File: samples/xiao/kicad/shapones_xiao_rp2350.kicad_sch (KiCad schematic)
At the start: 44 parts, among them Q1 PMOS, Q4 NMOS, SW1 POWER, SW10 MENU, SW2 A, SW3 B, SW4 SELECT, SW5 START, SW6 UP, SW7 DOWN, SW8 LEFT, SW9 RIGHT, U1 XIAO RP2350, U2 PCA9555D, U4 1.54''IPS-240x240, U5 TFCard, U6 74AHC1G04W5, U7 HT82V73A

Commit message: wip: PCB layout
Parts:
- removed BT1: Battery_Cell, symbol Device:Battery_Cell
- removed C6: 1u, symbol Device:C_Small
- removed LS1: 8ohm, symbol Device:Speaker
- removed SW1: POWER, symbol Switch:SW_Push
- removed SW10: MENU, symbol Switch:SW_Push
- removed SW2: A, symbol Switch:SW_Push
- removed SW3: B, symbol Switch:SW_Push
- removed SW4: SELECT, symbol Switch:SW_Push
- removed SW5: START, symbol Switch:SW_Push
- removed SW6: UP, symbol Switch:SW_Push
- removed SW7: DOWN, symbol Switch:SW_Push
- removed SW8: LEFT, symbol Switch:SW_Push
- removed SW9: RIGHT, symbol Switch:SW_Push
- removed U1: XIAO RP2350, symbol shpc_modules:RaspberryPiPico
- removed U2: PCA9555D, Package_SO:SOIC-24W_7.5x15.4mm_P1.27mm, symbol Interface_Expansion:PCA9555D
- removed U4: 1.54''IPS-240x240, symbol shpc_modules:RaspberryPiPico
- removed U5: TFCard, symbol shpc_modules:RaspberryPiPico
- removed U6: 74AHC1G04W5, Package_TO_SOT_SMD:SOT-553, symbol 74xGxx:74LVC1GU04DRL
- removed U7: HT82V73A, Package_SO:JEITA_SOIC-8_3.9x4.9mm_P1.27mm, symbol Amplifier_Audio:IS31AP4991-GRLS2
- added C11, C4: 1u, Capacitor_SMD:C_0402_1005Metric, symbol Device:C_Small
- added C2: 4.7u, Capacitor_SMD:C_0603_1608Metric, symbol Device:C_Small
- added C5: 4.7u, Capacitor_SMD:C_0402_1005Metric, symbol Device:C_Small
- added D4, D6, D8: 1N4148WS, Diode_SMD:D_SOD-323, symbol Device:D_Small
- added D5: YLED0402B, LED_SMD:LED_0402_1005Metric, symbol Device:LED_Small
- added D9: YLED0402O, LED_SMD:LED_0402_1005Metric, symbol Device:LED_Small
- added FB2: BLM21PG331SN1D, Inductor_SMD:L_Walsin_WLFM201209x, symbol Device:FerriteBead_Small
- added J1: JST S2B-PH-SM4-TB, Connector_JST:JST_PH_S2B-PH-SM4-TB_1x02-1MP_P2.00mm_Horizontal, symbol Connector_Generic_MountingPin:Conn_01x02_MountingPin
- added J3: Micro_SD_Card_Det_Hirose_DM3AT, Connector_Card:microSD_HC_Hirose_DM3AT-SF-PEJM5, symbol Connector:Micro_SD_Card_Det_Hirose_DM3AT
- added J4: Hong Cheng HC-PM254-5.0H-2x10PS, Connector_PinSocket_2.54mm:PinSocket_2x10_P2.54mm_Vertical_SMD, symbol Connector_Generic:Conn_02x10_Odd_Even
- added J5, J6: Conn_01x01, Connector_Wire:SolderWirePad_1x01_SMD_2x4mm, symbol Connector_Generic:Conn_01x01
- added Q2: IRLML6344TRPBF, Package_TO_SOT_SMD:SOT-23, symbol Simulation_SPICE:NMOS
- added Q4: IRLML2246TRPBF, Package_TO_SOT_SMD:SOT-23, symbol Simulation_SPICE:PMOS
- added R11, R23, R24, R25: 0, Resistor_SMD:R_0402_1005Metric, symbol Device:R_Small
- added R16, R21, R42, R5, R8: 10k, Resistor_SMD:R_0402_1005Metric, symbol Device:R_Small
- added R18: 2.2k, Resistor_SMD:R_0402_1005Metric, symbol Device:R_Small
- added R2, R9: 100, Resistor_SMD:R_0402_1005Metric, symbol Device:R_Small
- added R20: 22k, Resistor_SMD:R_0402_1005Metric, symbol Device:R_Small
- added R22, R7: 100k, Resistor_SMD:R_0402_1005Metric, symbol Device:R_Small
- added RV1: RK10J12E0A0A, shpc_mechanical:RK10J1xE, symbol shpc_mechanical:RK10J12E0A0A
- added SW1, SW10: GT-TC018A-H0375-L1, shpc_mechanical:GT-TC018A-H0375-L1, symbol Switch:SW_Push_Shielded
- added SW2, SW3, SW4, SW5, SW6, SW7, SW8, SW9: Rubber, shpc_mechanical:Rubber_Contact, symbol shpc_mechanical:Rubber_Contact
- added U1: XIAO RP2350, shpc_modules:XIAO RP2350, symbol shpc_modules:XIAO_RP2350
- added U2: RT9080-33GJ5, Package_TO_SOT_SMD:TSOT-23-5, symbol shpc_ic:RT9080-33GJ5
- added U3: 74VHC1G126, Package_TO_SOT_SMD:SOT-23-5, symbol shpc_ic:MC74VHC1G126DTT1G-TP
- added U4: HT82V73A, shpc_ic:SOIC-8_with_Thermal_Hole, symbol shpc_ic:HT82V73A
- added U5: PCA9555PW, Package_SO:TSSOP-24_4.4x7.8mm_P0.65mm, symbol Interface_Expansion:PCA9555PW
- added U6: M154-240240-RGB, shpc_modules:M154-240240-RGB, symbol shpc_modules:M154-240240-RGB
- C1: footprint (none) -> Capacitor_SMD:C_0603_1608Metric
- C10: renamed from C3; footprint (none) -> Capacitor_SMD:C_0402_1005Metric
- C3: renamed from C2; footprint (none) -> Capacitor_SMD:C_0402_1005Metric
- C6: renamed from C4; footprint (none) -> Capacitor_SMD:C_0402_1005Metric
- C7: renamed from C5; footprint (none) -> Capacitor_SMD:C_0402_1005Metric
- C8: renamed from C7; footprint (none) -> Capacitor_SMD:C_0603_1608Metric
- C9: renamed from C8; footprint (none) -> Capacitor_SMD:C_0603_1608Metric
- D1, D2, D3: value 1N4148W -> 1N4148WS; footprint (none) -> Diode_SMD:D_SOD-323; LCSC (none) -> C60580
- Q1: renamed from Q4; value NMOS -> IRLML6344TRPBF; footprint (none) -> Package_TO_SOT_SMD:SOT-23; LCSC (none) -> C53550
- Q3: renamed from Q1; value PMOS -> IRLML2246TRPBF; footprint (none) -> Package_TO_SOT_SMD:SOT-23; LCSC (none) -> C127272
- R1, R4: footprint (none) -> Resistor_SMD:R_0402_1005Metric
- R12: renamed from R8; footprint (none) -> Resistor_SMD:R_0402_1005Metric
- R13: renamed from R9; footprint (none) -> Resistor_SMD:R_0402_1005Metric; now not fitted
- R14: renamed from R10; footprint (none) -> Resistor_SMD:R_0402_1005Metric; now not fitted
- R15: renamed from R11; footprint (none) -> Resistor_SMD:R_0402_1005Metric; now not fitted
- R17: renamed from R12; footprint (none) -> Resistor_SMD:R_0402_1005Metric
- R19: renamed from R25; footprint (none) -> Resistor_SMD:R_0402_1005Metric
- R26, R28: value 10k -> 0; footprint (none) -> Resistor_SMD:R_0402_1005Metric
- R27: value 2.2k -> 0; footprint (none) -> Resistor_SMD:R_0402_1005Metric; now not fitted
- R3: renamed from R2; footprint (none) -> Resistor_SMD:R_0402_1005Metric
- R6: renamed from R3; footprint (none) -> Resistor_SMD:R_0402_1005Metric
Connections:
- net MISO is gone; now on net LCD_CS: R12.2
- net +3V3: now also R27.1, C2.1, J4.2 (Pin_2), R23.1, R25.1, SW1.1, U1.12 (3V3), U5.24 (VDD)
- net GND: now also D3.2 (A), R26.2, C11.2, C4.2, C5.2, D5.1 (K), J1.MP (MountPin), J3.11 (SHIELD), J3.6 (VSS), J4.17 (Pin_17), J4.4 (Pin_4), Q2.3 (S), R22.2, R24.2, R7.2, RV1.1, RV1.2B, RV1.3B, SW1.SH (B), SW10.2, SW10.SH (B), SW2.2, SW3.2, SW4.2, SW5.2, SW6.2, SW7.2, SW8.2, SW9.2, U1.13 (GND), U2.2 (GND), U2.4 (NC), U3.3 (GND), U4.4 (VSS), U5.12 (VSS), U6.1 (GND), U6.MP; no longer D2.2 (A), R27.2
- net LCD_CS: now also J4.11 (Pin_11), U1.4 (GP5), U6.7 (CS); no longer R17.2
- net LCD_DC: now also J4.10 (Pin_10), U1.3 (GP28), U6.6 (DC)
- net SOUND: now also U1.8 (GP1), U3.2
- net SW_DOWN: now also D2.1 (K), SW4.1, U5.18 (IO1_5); no longer D3.1 (K)
- net VPERI: now also J3.4 (VDD), J4.1 (Pin_1), R16.1, R21.1, R8.1, U2.3 (EN), U6.2 (VCC), U6.8 (BLK); no longer C6.2, C8.2
- net at D1.1 (K), R1.1, R3.1: now also R2.2, SW1.2
- net at R4.2: now also D2.2 (A); no longer D3.2 (A)
- net at R28.1: now also R27.2, U5.3 (A2)
- net at C9.2: now also U4.3 (VREF)
- net at C1.1, D1.2 (A), Q1.2 (G)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: now also D3.1 (K); no longer D2.1 (K)
- net at C7.1, R19.2: now also R18.2, R20.1; no longer R26.1
- net at R19.1: now also U3.4
- net BOOTSEL: no longer names the net of R4.1
- net BOOTSEL: now also U1.15 (BOOT)
- net CLK renamed SPI_MOSI
- net SPI_MOSI: now also J3.3 (CMD), J4.8 (Pin_8), U1.11 (GP3), U6.4 (SDA)
- net MOSI renamed SPI_SCK
- net SPI_SCK: now also J3.5 (CLK), J4.7 (Pin_7), U1.9 (GP2), U6.3 (SCL)
- net PERI_EN: no longer names the net of Q3.2 (G), R6.2
- net PERI_EN: now also C2.2, D4.2 (A), Q2.1 (D)
- net RESET: no longer names the net of Q1.1 (D)
- net RESET: now also U1.16 (RST)
- net TF_CS: no longer names the net of R13.2
- net TF_CS: now also R11.2, U6.5 (RES)
- new net: J6.1 (Pin_1), U4.1
- new net: RV1.2A, U4.2 (IN)
- new net: D8.1 (K), R22.1, R42.2, U4.5 (~{CE})
- new net: J5.1 (Pin_1), U4.7
- new net: Q2.2 (G), R5.1, R7.1
- new net: R20.2, RV1.3A
- new net: C11.1, FB2.2, U2.1 (VIN)
- new net: D9.2 (A), R21.2
- new net: R23.2, R24.1, U5.21 (A0)
- new net: Q4.2 (G), R9.2
- new net: R25.2, R26.1, U5.2 (A1)
- new net: D5.2 (A), R8.2
- new net: R2.1, U1.2 (GP27)
- new net +BAT: J1.1 (Pin_1), Q4.1 (D), U1.18 (BAT+)
- new net -BAT: J1.2 (Pin_2), U1.17 (BAT-)
- new net EXT_AUDIO: J4.20 (Pin_20), R18.1
- new net EXT_MUTE: D8.2 (A), J4.19 (Pin_19)
- new net I2C_SCL: J4.12 (Pin_12), R5.2, U1.6 (GP7), U5.22 (SCL)
- new net I2C_SDA: J4.13 (Pin_13), U1.5 (GP6), U5.23 (SDA)
- new net IOEX0: J4.14 (Pin_14), U5.4 (IO0_0)
- new net IOEX1: J4.15 (Pin_15), U5.5 (IO0_1)
- new net IOEX2: J4.16 (Pin_16), U5.6 (IO0_2)
- new net IOEX3: J4.18 (Pin_18), U5.7 (IO0_3)
- new net LCD_RESET_N: R11.1, U5.9 (IO0_5)
- new net MUTE_INT: R42.1, U5.10 (IO0_6)
- new net PERI_EN_N: D4.1 (K), U5.8 (IO0_4)
- new net SPI_MISO: J3.7 (DAT0), J4.9 (Pin_9), R17.2, U1.10 (GP4)
- new net SW_A: SW9.1, U5.13 (IO1_0)
- new net SW_B: SW8.1, U5.14 (IO1_1)
- new net SW_LEFT: SW3.1, U5.19 (IO1_6)
- new net SW_MENU: SW10.1, U5.11 (IO0_7)
- new net SW_RIGHT: SW2.1, U5.20 (IO1_7)
- new net SW_SELECT: SW7.1, U5.15 (IO1_2)
- new net SW_START: SW6.1, U5.16 (IO1_3)
- new net SW_UP: SW5.1, U5.17 (IO1_4)
- new net TFC_CS: D9.1 (K), J3.2 (DAT3/CD), R16.2, U1.7 (GP0)
- new net VANL: C5.1, C6.2, C8.2, U2.5 (VOUT), U3.1, U3.5 (VCC), U4.8 (VDD)
- new net VBUS: D6.2 (A), J4.6 (Pin_6), R9.1, U1.14 (VBUS)
- new net VCOM: C4.1, D6.1 (K), FB2.1, J4.3 (Pin_3), Q4.3 (S)
- new net XIAO_GPIO: J4.5 (Pin_5), U1.1 (GP26)
- no-connect marks 7 -> 5
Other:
- note added: "A"
- note added: "B"
- note added: "BATTERY"
- note added: "DOWN"
- note added: "EXT_PORT"
- note added: "LEFT"
- note added: "MENU"
- note added: "POWER"
- note added: "RIGHT"
- note added: "SELECT"
- note added: "SPEAKER"
- note added: "START"
- note added: "UP"
- moved on the sheet: C1, C10, C3, C6, C7, C8, C9, D1, Q1, Q3, R1, R12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

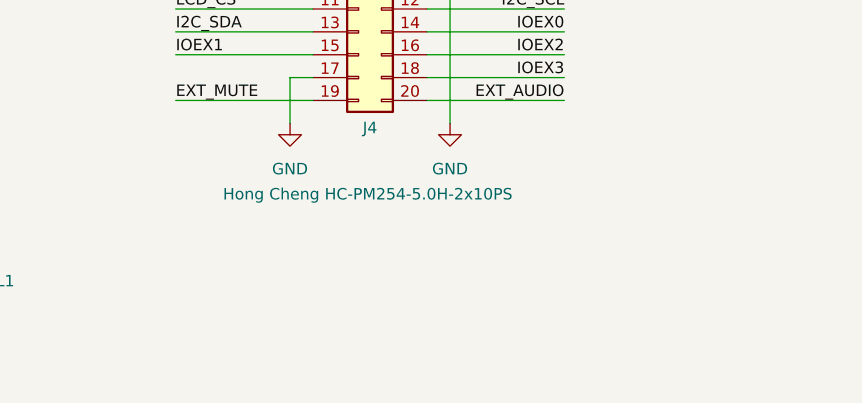
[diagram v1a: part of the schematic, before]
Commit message: add tooling strips
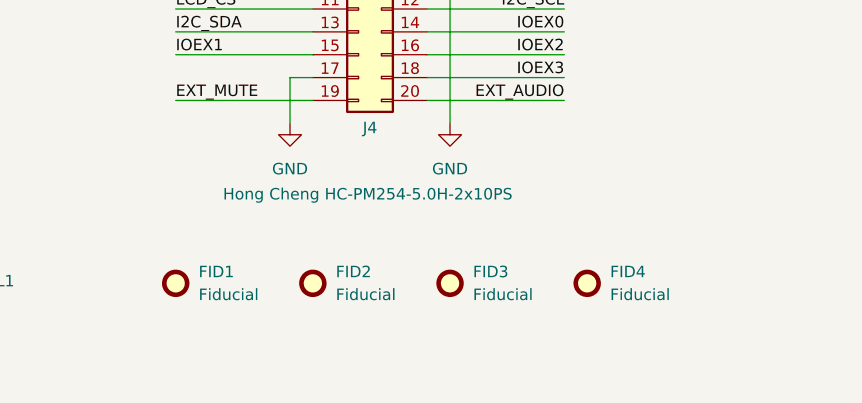
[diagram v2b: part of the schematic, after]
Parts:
- added FID1, FID2, FID3, FID4: Fiducial, Fiducial:Fiducial_1mm_Mask2mm, symbol Mechanical:Fiducial
- C1, C2: LCSC (none) -> C1705; URL (none) -> https://www.lcsc.com/product-detail/C1705.html
- C10, C6: LCSC (none) -> C1525; URL (none) -> https://www.lcsc.com/product-detail/C1525.html
- C11, C3, C4: LCSC (none) -> C14445; URL (none) -> https://www.lcsc.com/product-detail/C14445.html
- C5: footprint Capacitor_SMD:C_0402_1005Metric -> Capacitor_SMD:C_0603_1608Metric; LCSC (none) -> C1705; URL (none) -> https://www.lcsc.com/product-detail/C1705.html
- C7: LCSC (none) -> C15195; URL (none) -> https://www.lcsc.com/product-detail/C15195.html
- C8: LCSC (none) -> C140782; URL (none) -> https://www.lcsc.com/product-detail/C140782.html
- C9: LCSC (none) -> C1691; URL (none) -> https://www.lcsc.com/product-detail/C1691.html
- R1, R12, R13, R14, R16, R17, R21, R42, R5, R8: LCSC (none) -> C60490; URL (none) -> https://www.lcsc.com/product-detail/C60490.html
- R11, R23, R24, R25, R26, R27, R28: LCSC (none) -> C106231; URL (none) -> https://www.lcsc.com/product-detail/C106231.html
- R15: LCSC (none) -> C60489; URL (none) -> https://www.lcsc.com/product-detail/C60489.html
- R18, R19: LCSC (none) -> C114762; URL (none) -> https://www.lcsc.com/product-detail/C114762.html
- R2, R9: LCSC (none) -> C1545; URL (none) -> https://www.lcsc.com/product-detail/C1545.html
- R20: LCSC (none) -> C82868; URL (none) -> https://www.lcsc.com/product-detail/C82868.html
- R22, R6, R7: LCSC (none) -> C60491; URL (none) -> https://www.lcsc.com/product-detail/C60491.html
- R3: LCSC (none) -> C137976; URL (none) -> https://www.lcsc.com/product-detail/C137976.html
- R4: LCSC (none) -> C106235; URL (none) -> https://www.lcsc.com/product-detail/C106235.html

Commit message: Orders made to JLCPCB
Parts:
- removed FID1, FID2, FID3, FID4: Fiducial, Fiducial:Fiducial_1mm_Mask2mm, symbol Mechanical:Fiducial
- removed J5, J6: Conn_01x01, Connector_Wire:SolderWirePad_1x01_SMD_2x4mm, symbol Connector_Generic:Conn_01x01
- added J2: Conn_01x02, shpc_mechanical:SolderWirePad_1x02_SMD_150x50mil, symbol Connector_Generic:Conn_01x02
- D1, D2, D3, D4, D6, D8: URL (none) -> https://www.lcsc.com/product-detail/C60580.html
- D5: URL (none) -> https://www.lcsc.com/product-detail/C30584803.html
- D9: URL (none) -> https://www.lcsc.com/product-detail/C28310436.html
- FB2: footprint Inductor_SMD:L_Walsin_WLFM201209x -> Inductor_SMD:L_0805_2012Metric; URL (none) -> https://www.lcsc.com/product-detail/C74764.html
- J1: URL (none) -> https://www.lcsc.com/product-detail/C295747.html
- J3: URL (none) -> https://www.lcsc.com/product-detail/C114218.html
- J4: URL (none) -> https://www.lcsc.com/product-detail/C42163138.html
- Q1, Q2: URL (none) -> https://www.lcsc.com/product-detail/C53550.html
- Q3, Q4: URL (none) -> https://www.lcsc.com/product-detail/C127272.html
- R15: LCSC C60489 -> C60490; URL https://www.lcsc.com/product-detail/C60489.html -> https://www.lcsc.com/product-detail/C60490.html
- RV1: URL (none) -> https://www.lcsc.com/product-detail/C351176.html
- SW1, SW10: URL (none) -> https://www.lcsc.com/product-detail/C963235.html
- U2: URL (none) -> https://www.lcsc.com/product-detail/C841192.html
- U3: URL (none) -> https://www.lcsc.com/product-detail/C53100485.html
- U5: URL (none) -> https://www.lcsc.com/product-detail/C128392.html
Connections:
- net I2C_SCL: now also J4.13 (Pin_13); no longer J4.12 (Pin_12)
- net I2C_SDA: now also J4.12 (Pin_12); no longer J4.13 (Pin_13)
- net at U4.1: now also J2.2 (Pin_2)
- net at U4.7: now also J2.1 (Pin_1)
- net IOEX_A2: now reaches R27.2, R28.1, U5.3 (A2)
- net IOEX_A0: now reaches R23.2, R24.1, U5.21 (A0)
- net IOEX_A1: now reaches R25.2, R26.1, U5.2 (A1)
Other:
- moved on the sheet: R23, R24, R25, R26, R27, R28

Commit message: fix
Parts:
- R22: now fitted
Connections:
- net MUTE_INT renamed INT_MUTE
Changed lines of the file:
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@@
 		)
 	)
-	(label "MUTE_INT"
+	(label "INT_MUTE"
 		(at 88.9 154.94 0)
 		(effects
@@
 		)
 	)
-	(label "MUTE_INT"
+	(label "INT_MUTE"
 		(at 99.06 213.36 180)
 		(effects
@@
 		(in_bom yes)
 		(on_board yes)
-		(dnp yes)
+		(dnp no)
 		(property "Reference" "R22"
 			(at 120.65 137.16 90)

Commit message: fix
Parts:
- removed D4, D8: 1N4148WS, Diode_SMD:D_SOD-323, symbol Device:D_Small
- removed R42: 10k, Resistor_SMD:R_0402_1005Metric, symbol Device:R_Small
- added Q5: IRLML2246TRPBF, Package_TO_SOT_SMD:SOT-23, symbol Simulation_SPICE:PMOS
- added R10: 100k, Resistor_SMD:R_0402_1005Metric, symbol Device:R_Small
- added R29, R30: 10k, Resistor_SMD:R_0402_1005Metric, symbol Device:R_Small
- R5: value 10k -> 100k
- R7: value 100k -> 1M
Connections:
- net +3V3: now also R29.1, R30.1
- net EXT_MUTE: now also Q5.2 (G), R10.2
- net GND: now also R10.1; no longer Q2.3 (S), R22.2, R7.2
- net I2C_SCL: now also R29.2
- net I2C_SDA: now also R30.2
- net INT_MUTE: now also Q5.1 (D)
- net PERI_EN_N: now also Q2.3 (S), R7.2
- net VANL: now also R22.2
- net at R22.1, U4.5 (~{CE}): now also Q5.3 (S)
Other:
- moved on the sheet: C1, C11, C2, C3, C4, C5, D1, D2, D3, D5, D6, FB2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

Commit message: fix
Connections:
- net EXT_MUTE: no longer J4.19 (Pin_19), Q5.2 (G), R10.2
- net INT_MUTE renamed IOEX_MUTE
- new net SPK_MUTE: J4.19 (Pin_19), Q5.2 (G), R10.2
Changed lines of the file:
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@@
 		)
 	)
-	(label "INT_MUTE"
+	(label "IOEX_MUTE"
 		(at 99.06 213.36 180)
 		(effects
@@
 		)
 	)
-	(label "EXT_MUTE"
+	(label "SPK_MUTE"
 		(at 215.9 233.68 0)
 		(effects
@@
 		)
 	)
-	(label "EXT_MUTE"
+	(label "SPK_MUTE"
 		(at 88.9 154.94 0)
 		(effects
@@
 		)
 	)
-	(label "INT_MUTE"
+	(label "IOEX_MUTE"
 		(at 88.9 175.26 0)
 		(effects

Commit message: fix
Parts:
- removed R11: 0, Resistor_SMD:R_0402_1005Metric, symbol Device:R_Small
- added D4, D7: 1N4148WS, Diode_SMD:D_SOD-323, symbol Device:D_Small
- R13: now fitted
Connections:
- net IOEX_MUTE: now also D4.1 (K); no longer Q5.1 (D)
- net LCD_RESET_N: now also D7.1 (K)
- net at R13.2, U6.5 (RES): now also D7.2 (A)
- new net: D4.2 (A), Q5.1 (D)
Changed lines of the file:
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@@
 	(wire
 		(pts
-			(xy 88.9 175.26) (xy 115.57 175.26)
+			(xy 88.9 175.26) (xy 101.6 175.26)
 		)
 		(stroke
@@
 	(wire
 		(pts
+			(xy 106.68 175.26) (xy 115.57 175.26)
+		)
+		(stroke
+			(width 0)
+			(type default)
+		)
+	)
+	(wire
+		(pts
 			(xy 40.64 73.66) (xy 45.72 73.66)
 		)
@@
 	)
 	(symbol
-		(lib_id "power:+3V3")
-		(at 129.54 30.48 0)
+		(lib_id "Device:D_Small")
+		(at 195.58 121.92 0)
+		(mirror x)
 		(unit 1)
 		(exclude_from_sim no)
@@
 		(on_board yes)
 		(dnp no)
-		(fields_autoplaced yes)
-		(property "Reference" "#PWR06"
-			(at 129.54 34.29 0)
+		(property "Reference" "D7"
+			(at 194.056 124.714 0)
+			(effects
+				(font
+					(size 1.27 1.27)
+				)
+			)
+		)
+		(property "Value" "1N4148WS"
+			(at 197.866 126.746 0)
+			(effects
+				(font
+					(size 1.27 1.27)
+				)
+			)
+		)
+		(property "Footprint" "Diode_SMD:D_SOD-323"
+			(at 195.58 121.92 90)
 			(effects
 				(font
@@
 			)
 		)
-		(property "Value" "VBUS"
-			(at 129.54 25.4 0)
+		(property "Datasheet" "~"
+			(at 195.58 121.92 90)
 			(effects
 				(font
 					(size 1.27 1.27)
 				)
+				(hide yes)
 			)
 		)
-		(property "Footprint" ""
-			(at 129.54 30.48 0)
+		(property "Description" "Diode, small symbol"
+			(at 195.58 121.92 0)
 			(effects
 				(font
@@
 			)
 		)
-		(property "Datasheet" ""
-			(at 129.54 30.48 0)
+		(property "Sim.Device" "D"
+			(at 195.58 121.92 0)
 			(effects
 				(font
@@
 			)
 		)
-		(property "Description" "Power symbol creates a global label with name \"+3V3\""
-			(at 129.54 30.48 0)
+		(property "Sim.Pins" "1=K 2=A"
+			(at 195.58 121.92 0)
+			(effects
+				(font
+					(size 1.27 1.27)
+				)
+				(hide yes)
+			)
+		)
+		(property "LCSC" "C60580"
+			(at 195.58 121.92 0)
+			(effects
+				(font
+					(size 1.27 1.27)
+				)
+				(hide yes)
+			)
+		)
+		(property "URL" "https://www.lcsc.com/product-detail/C60580.html"
+			(at 195.58 121.92 0)
 			(effects
 				(font
@@
 			)
 		)
+		(pin "2"
+		)
 		(pin "1"
 		)
@@
 			(project "shapones_xiao_rp2350"
 				(path "/c325fb4c-906a-4010-8224-fd2c0e1f0539"
-					(reference "#PWR06")
+					(reference "D7")
 					(unit 1)
 				)
@@
 	)
 	(symbol
-		(lib_id "Device:R_Small")
-		(at 172.72 35.56 0)
-		(mirror y)
+		(lib_id "power:+3V3")
+		(at 129.54 30.48 0)
 		(unit 1)
 		(exclude_from_sim no)
@@
 		(on_board yes)
 		(dnp no)
-		(property "Reference" "R6"
-			(at 171.45 34.29 0)
-			(effects
-				(font
-					(size 1.016 1.016)
-				)
-				(justify left)
-			)
-		)
-		(property "Value" "100k"
-			(at 171.45 36.83 0)
-			(effects
-				(font
-					(size 1.27 1.27)
-				)
-				(justify left)
-			)
-		)
-		(property "Footprint" "Resistor_SMD:R_0402_1005Metric"
-			(at 172.72 35.56 0)
+		(fields_autoplaced yes)
+		(property "Reference" "#PWR06"
+			(at 129.54 34.29 0)
 			(effects
 				(font
@@
 			)
 		)
-		(property "Datasheet" "~"
-			(at 172.72 35.56 0)
+		(property "Value" "VBUS"
+			(at 129.54 25.4 0)
 			(effects
 				(font
 					(size 1.27 1.27)
 				)
-				(hide yes)
 			)
 		)
-		(property "Description" "Resistor, small symbol"
-			(at 172.72 35.56 0)
+		(property "Footprint" ""
+			(at 129.54 30.48 0)
 			(effects
 				(font
@@
 			)
 		)
-		(property "LCSC" "C60491"
-			(at 171.45 34.29 0)
+		(property "Datasheet" ""
+			(at 129.54 30.48 0)
 			(effects
 				(font
@@
 			)
 		)
-		(property "URL" "https://www.lcsc.com/product-detail/C60491.html"
-			(at 171.45 34.29 0)
+		(property "Description" "Power symbol creates a global label with name \"+3V3\""
+			(at 129.54 30.48 0)
 			(effects
 				(font
@@
 		(pin "1"
 		)
-		(pin "2"
-		)
 		(instances
 			(project "shapones_xiao_rp2350"
 				(path "/c325fb4c-906a-4010-8224-fd2c0e1f0539"
-					(reference "R6")
+					(reference "#PWR06")
 					(unit 1)
 				)
@@
 	(symbol
 		(lib_id "Device:R_Small")
-		(at 195.58 121.92 90)
+		(at 172.72 35.56 0)
+		(mirror y)
 		(unit 1)
 		(exclude_from_sim no)
@@
 		(on_board yes)
 		(dnp no)
-		(property "Reference" "R11"
-			(at 195.58 124.206 90)
+		(property "Reference" "R6"
+			(at 171.45 34.29 0)
 			(effects
 				(font
 					(size 1.016 1.016)
 				)
+				(justify left)
 			)
 		)
-		(property "Value" "0"
-			(at 195.58 126.492 90)
+		(property "Value" "100k"
+			(at 171.45 36.83 0)
 			(effects
 				(font
 					(size 1.27 1.27)
 				)
+				(justify left)
 			)
 		)
 		(property "Footprint" "Resistor_SMD:R_0402_1005Metric"
-			(at 195.58 121.92 0)
+			(at 172.72 35.56 0)
 			(effects
 				(font
@@
 		)
 		(property "Datasheet" "~"
-			(at 195.58 121.92 0)
+			(at 172.72 35.56 0)
 			(effects
 				(font
@@
 		)
 		(property "Description" "Resistor, small symbol"
-			(at 195.58 121.92 0)
+			(at 172.72 35.56 0)
 			(effects
 				(font
@@
 			)
 		)
-		(property "LCSC" "C106231"
-			(at 195.58 124.206 90)
+		(property "LCSC" "C60491"
+			(at 171.45 34.29 0)
 			(effects
 				(font
@@
 			)
 		)
-		(property "URL" "https://www.lcsc.com/product-detail/C106231.html"
-			(at 195.58 124.206 90)
+		(property "URL" "https://www.lcsc.com/product-detail/C60491.html"
+			(at 171.45 34.29 0)
 			(effects
 				(font
@@
 			(project "shapones_xiao_rp2350"
 				(path "/c325fb4c-906a-4010-8224-fd2c0e1f0539"
-					(reference "R11")
+					(reference "R6")
 					(unit 1)
 				)
@@
 		(in_bom yes)
 		(on_board yes)
-		(dnp yes)
+		(dnp no)
 		(property "Reference" "R13"
 			(at 201.168 112.268 0)
@@
 					(unit 1)
 				)
+			)
+		)
+	)
+	(symbol
+		(lib_id "Device:D_Small")
+		(at 104.14 175.26 0)
+		(mirror x)
+		(unit 1)
+		(exclude_from_sim no)
+		(in_bom yes)
+		(on_board yes)
+		(dnp no)
+		(property "Reference" "D4"
+			(at 104.14 178.308 0)
+			(effects
+				(font
+					(size 1.27 1.27)
+				)
+			)
+		)
+		(property "Value" "1N4148WS"
+			(at 104.14 180.34 0)
+			(effects
+				(font
+					(size 1.27 1.27)
+				)
+			)
+		)
+		(property "Footprint" "Diode_SMD:D_SOD-323"
+			(at 104.14 175.26 90)
+			(effects
+				(font
+					(size 1.27 1.27)
+				)
+				(hide yes)
+			)
+		)
+		(property "Datasheet" "~"
+			(at 104.14 175.26 90)
+			(effects
+				(font
+					(size 1.27 1.27)
+				)
+				(hide yes)
+			)
+		)
+		(property "Description" "Diode, small symbol"
+			(at 104.14 175.26 0)
+			(effects
+				(font
+					(size 1.27 1.27)
+				)
+				(hide yes)
+			)
+		)
+		(property "Sim.Device" "D"
+			(at 104.14 175.26 0)
+			(effects
+				(font
+					(size 1.27 1.27)
+				)
+				(hide yes)
+			)
+		)
+		(property "Sim.Pins" "1=K 2=A"
+			(at 104.14 175.26 0)
+			(effects
+				(font
+					(size 1.27 1.27)
+				)
+				(hide yes)
+			)
+		)
+		(property "LCSC" "C60580"
+			(at 104.14 175.26 0)
+			(effects
+				(font
+					(size 1.27 1.27)
+				)
+				(hide yes)
+			)
+		)
+		(property "URL" "https://www.lcsc.com/product-detail/C60580.html"
+			(at 104.14 175.26 0)
+			(effects
+				(font
+					(size 1.27 1.27)
+				)
+				(hide yes)
+			)
+		)
+		(pin "2"
+		)
+		(pin "1"
+		)
+		(instances
+			(project "shapones_xiao_rp2350"
+				(path "/c325fb4c-906a-4010-8224-fd2c0e1f0539"
+					(reference "D4")
+					(unit 1)
+				)

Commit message: fix
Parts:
- added C12: 1u, Capacitor_SMD:C_0603_1608Metric, symbol Device:C_Small
- added R11: 100k, Resistor_SMD:R_0402_1005Metric, symbol Device:R_Small
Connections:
- net GND: now also R11.2
- net SOUND: now also R11.1
- net at U4.2 (IN): now also C12.2; no longer RV1.2A
- new net: C12.1, RV1.2A
